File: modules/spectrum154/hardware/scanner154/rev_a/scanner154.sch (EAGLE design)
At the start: 7 parts, among them J1 TC2030-CC2538-BL, J2 MODULE_HEADER, U1 ATUM, U4 MAX8887EZK33+T

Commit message: update scanner module with silkscreen
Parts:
- removed U4: MAX8887EZK33+T, chips:MAX8887EZK33+T
- added LOGO2: UMICH_SOLID_HUGE, logos:UMICH_SOLID_HUGE
- added U2: MAX8887EZK33+T, chips:MAX8887EZK33+T
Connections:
- net GND: now also U2.GND; no longer U4.GND
- net N$11: now also U2.BP; no longer U4.BP
- net VBAT: now also U2.!SHDN, U2.IN; no longer U4.!SHDN, U4.IN
- net VCC: now also U2.OUT; no longer U4.OUT
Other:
- moved on the sheet: C1, C2, C3, J1, J2, U1

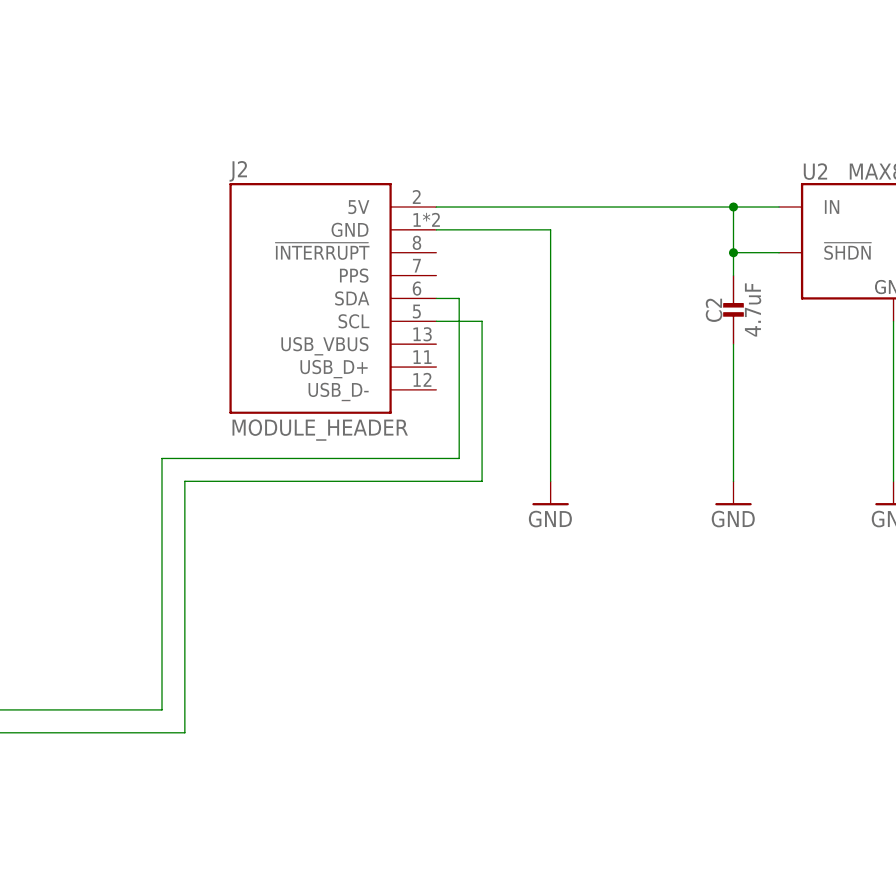
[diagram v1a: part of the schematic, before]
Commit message: Update scanner154 to new module header (add VCCIO)
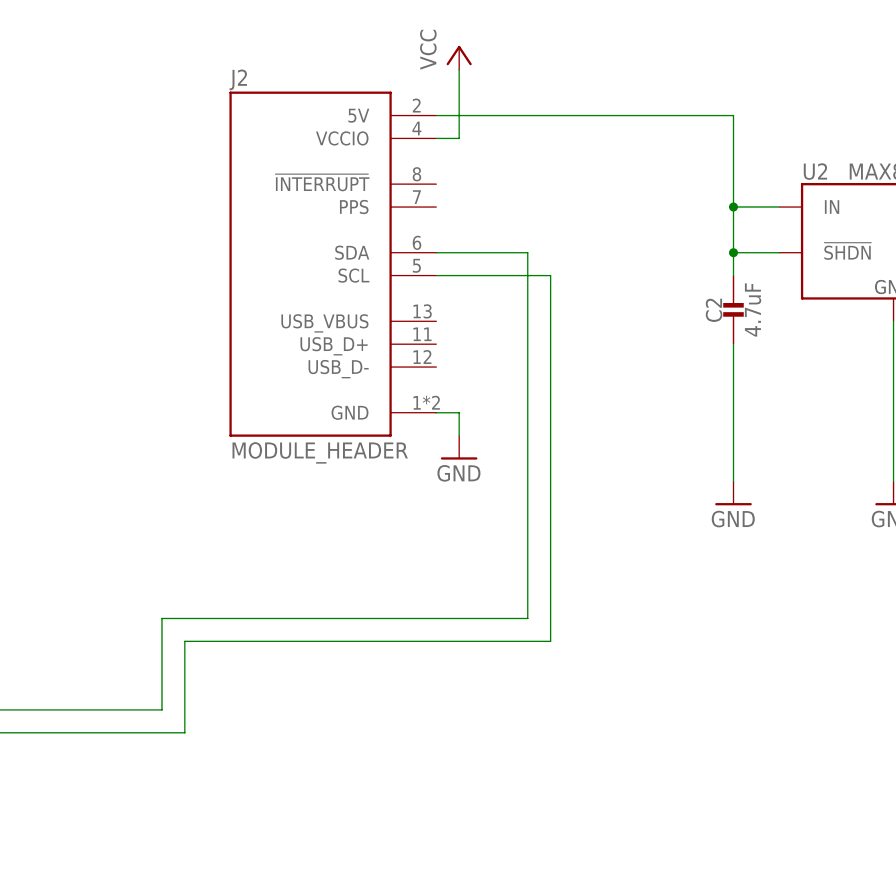
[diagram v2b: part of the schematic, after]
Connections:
- net VCC: now also J2.VCCIO
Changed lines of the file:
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@@
 <?xml version="1.0" encoding="utf-8"?>
 <!DOCTYPE eagle SYSTEM "eagle.dtd">
-<eagle version="6.5.0">
+<eagle version="6.4">
 <drawing>
 <settings>
@@
 <part name="C3" library="passives" deviceset="CAPACITOR" device="0603_CAP" value="4.7uF"/>
 <part name="LOGO2" library="logos" deviceset="UMICH_SOLID" device="_HUGE"/>
+<part name="P+4" library="supply1" deviceset="VCC" device=""/>
 </parts>
 <sheets>
@@
 <instance part="P+3" gate="VCC" x="43.18" y="152.4"/>
 <instance part="J2" gate="G$1" x="134.62" y="137.16"/>
-<instance part="SUPPLY3" gate="1" x="152.4" y="114.3"/>
+<instance part="SUPPLY3" gate="1" x="142.24" y="119.38"/>
 <instance part="C1" gate="G$1" x="205.74" y="137.16"/>
 <instance part="C2" gate="G$1" x="172.72" y="137.16"/>
 <instance part="C3" gate="G$1" x="215.9" y="137.16"/>
 <instance part="LOGO2" gate="G$1" x="231.14" y="25.4"/>
+<instance part="P+4" gate="VCC" x="142.24" y="165.1"/>
 </instances>
 <busses>
@@
 <segment>
 <pinref part="J2" gate="G$1" pin="GND"/>
-<wire x1="139.7" y1="144.78" x2="152.4" y2="144.78" width="0.1524" layer="91"/>
-<wire x1="152.4" y1="144.78" x2="152.4" y2="116.84" width="0.1524" layer="91"/>
+<wire x1="139.7" y1="124.46" x2="142.24" y2="124.46" width="0.1524" layer="91"/>
+<wire x1="142.24" y1="124.46" x2="142.24" y2="121.92" width="0.1524" layer="91"/>
 <pinref part="SUPPLY3" gate="1" pin="GND"/>
 </segment>
@@
 <wire x1="43.18" y1="147.32" x2="43.18" y2="149.86" width="0.1524" layer="91"/>
 <pinref part="P+3" gate="VCC" pin="VCC"/>
+</segment>
+<segment>
+<pinref part="J2" gate="G$1" pin="VCCIO"/>
+<pinref part="P+4" gate="VCC" pin="VCC"/>
+<wire x1="139.7" y1="154.94" x2="142.24" y2="154.94" width="0.1524" layer="91"/>
+<wire x1="142.24" y1="154.94" x2="142.24" y2="162.56" width="0.1524" layer="91"/>
 </segment>
 </net>
@@
 <junction x="172.72" y="142.24"/>
 <pinref part="J2" gate="G$1" pin="5V"/>
-<wire x1="172.72" y1="147.32" x2="139.7" y2="147.32" width="0.1524" layer="91"/>
+<wire x1="172.72" y1="147.32" x2="172.72" y2="157.48" width="0.1524" layer="91"/>
+<wire x1="172.72" y1="157.48" x2="139.7" y2="157.48" width="0.1524" layer="91"/>
 <pinref part="C2" gate="G$1" pin="1"/>
 </segment>
@@
 <segment>
 <pinref part="J2" gate="G$1" pin="SDA"/>
-<wire x1="139.7" y1="137.16" x2="142.24" y2="137.16" width="0.1524" layer="91"/>
-<wire x1="142.24" y1="137.16" x2="142.24" y2="119.38" width="0.1524" layer="91"/>
-<wire x1="142.24" y1="119.38" x2="109.22" y2="119.38" width="0.1524" layer="91"/>
-<wire x1="109.22" y1="119.38" x2="109.22" y2="91.44" width="0.1524" layer="91"/>
+<wire x1="139.7" y1="142.24" x2="149.86" y2="142.24" width="0.1524" layer="91"/>
+<wire x1="149.86" y1="142.24" x2="149.86" y2="101.6" width="0.1524" layer="91"/>
+<wire x1="149.86" y1="101.6" x2="109.22" y2="101.6" width="0.1524" layer="91"/>
+<wire x1="109.22" y1="101.6" x2="109.22" y2="91.44" width="0.1524" layer="91"/>
 <pinref part="U1" gate="G$1" pin="I2C_SDA"/>
 <wire x1="109.22" y1="91.44" x2="81.28" y2="91.44" width="0.1524" layer="91"/>
@@
 <segment>
 <pinref part="J2" gate="G$1" pin="SCL"/>
-<wire x1="139.7" y1="134.62" x2="144.78" y2="134.62" width="0.1524" layer="91"/>
-<wire x1="144.78" y1="134.62" x2="144.78" y2="116.84" width="0.1524" layer="91"/>
-<wire x1="144.78" y1="116.84" x2="111.76" y2="116.84" width="0.1524" layer="91"/>
-<wire x1="111.76" y1="116.84" x2="111.76" y2="88.9" width="0.1524" layer="91"/>
+<wire x1="139.7" y1="139.7" x2="152.4" y2="139.7" width="0.1524" layer="91"/>
+<wire x1="152.4" y1="139.7" x2="152.4" y2="99.06" width="0.1524" layer="91"/>
+<wire x1="152.4" y1="99.06" x2="111.76" y2="99.06" width="0.1524" layer="91"/>
+<wire x1="111.76" y1="99.06" x2="111.76" y2="88.9" width="0.1524" layer="91"/>
 <pinref part="U1" gate="G$1" pin="I2C_SCL"/>
 <wire x1="111.76" y1="88.9" x2="81.28" y2="88.9" width="0.1524" layer="91"/>

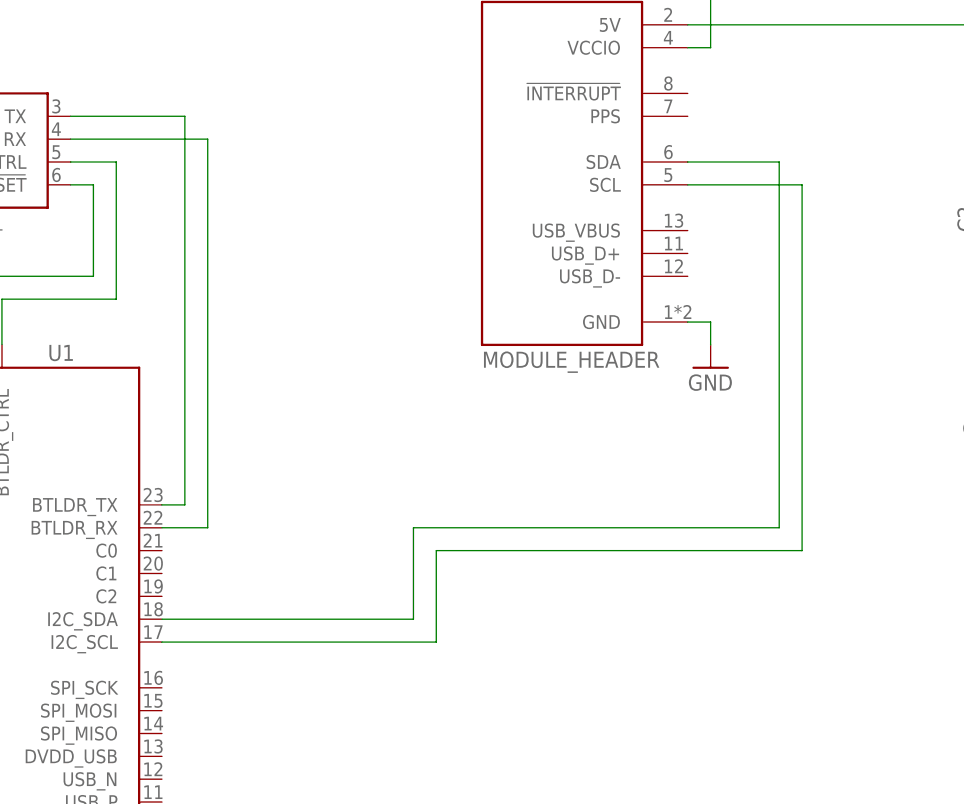
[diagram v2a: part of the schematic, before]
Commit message: moved some traces
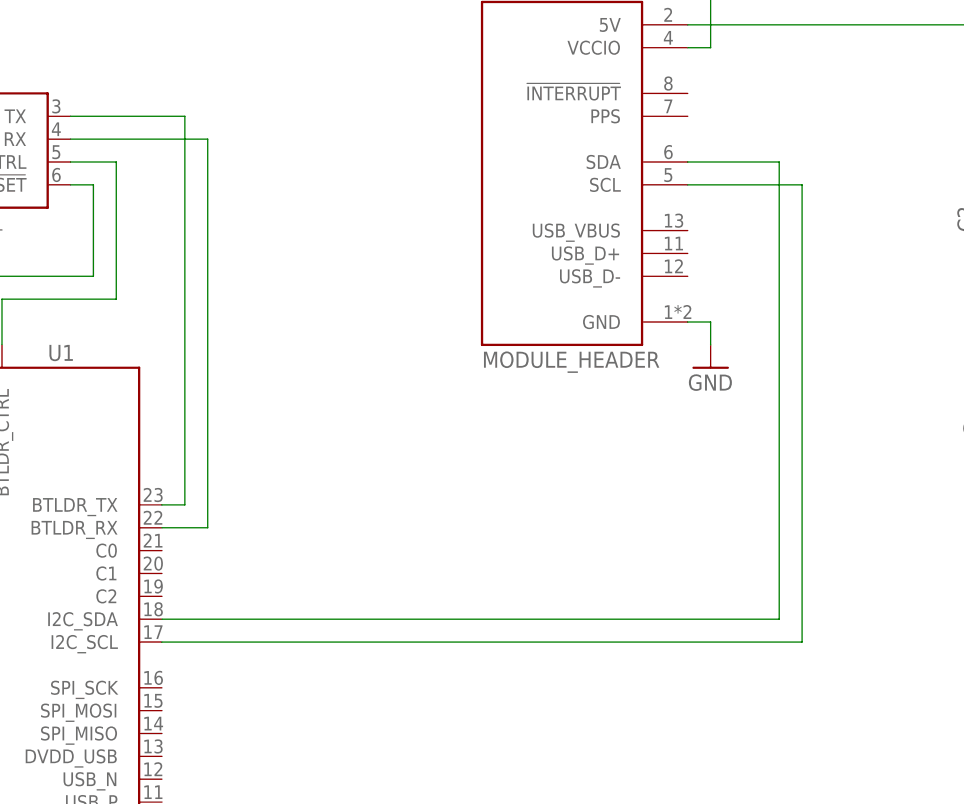
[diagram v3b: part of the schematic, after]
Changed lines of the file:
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@@
 <?xml version="1.0" encoding="utf-8"?>
 <!DOCTYPE eagle SYSTEM "eagle.dtd">
-<eagle version="6.4">
+<eagle version="6.5.0">
 <drawing>
 <settings>
@@
 <pinref part="J2" gate="G$1" pin="SDA"/>
 <wire x1="139.7" y1="142.24" x2="149.86" y2="142.24" width="0.1524" layer="91"/>
-<wire x1="149.86" y1="142.24" x2="149.86" y2="101.6" width="0.1524" layer="91"/>
-<wire x1="149.86" y1="101.6" x2="109.22" y2="101.6" width="0.1524" layer="91"/>
-<wire x1="109.22" y1="101.6" x2="109.22" y2="91.44" width="0.1524" layer="91"/>
+<wire x1="149.86" y1="142.24" x2="149.86" y2="91.44" width="0.1524" layer="91"/>
+<wire x1="149.86" y1="91.44" x2="81.28" y2="91.44" width="0.1524" layer="91"/>
 <pinref part="U1" gate="G$1" pin="I2C_SDA"/>
-<wire x1="109.22" y1="91.44" x2="81.28" y2="91.44" width="0.1524" layer="91"/>
 </segment>
 </net>
@@
 <pinref part="J2" gate="G$1" pin="SCL"/>
 <wire x1="139.7" y1="139.7" x2="152.4" y2="139.7" width="0.1524" layer="91"/>
-<wire x1="152.4" y1="139.7" x2="152.4" y2="99.06" width="0.1524" layer="91"/>
-<wire x1="152.4" y1="99.06" x2="111.76" y2="99.06" width="0.1524" layer="91"/>
-<wire x1="111.76" y1="99.06" x2="111.76" y2="88.9" width="0.1524" layer="91"/>
+<wire x1="152.4" y1="139.7" x2="152.4" y2="88.9" width="0.1524" layer="91"/>
+<wire x1="152.4" y1="88.9" x2="81.28" y2="88.9" width="0.1524" layer="91"/>
 <pinref part="U1" gate="G$1" pin="I2C_SCL"/>
-<wire x1="111.76" y1="88.9" x2="81.28" y2="88.9" width="0.1524" layer="91"/>
-</segment>
-</net>
+</segment>
+</net>
